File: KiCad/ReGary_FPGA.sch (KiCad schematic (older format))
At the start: 27 parts, among them U1 GW1N-UV1P5LQ100, U2 LM1117-3.3, U9 TPS73643DBV

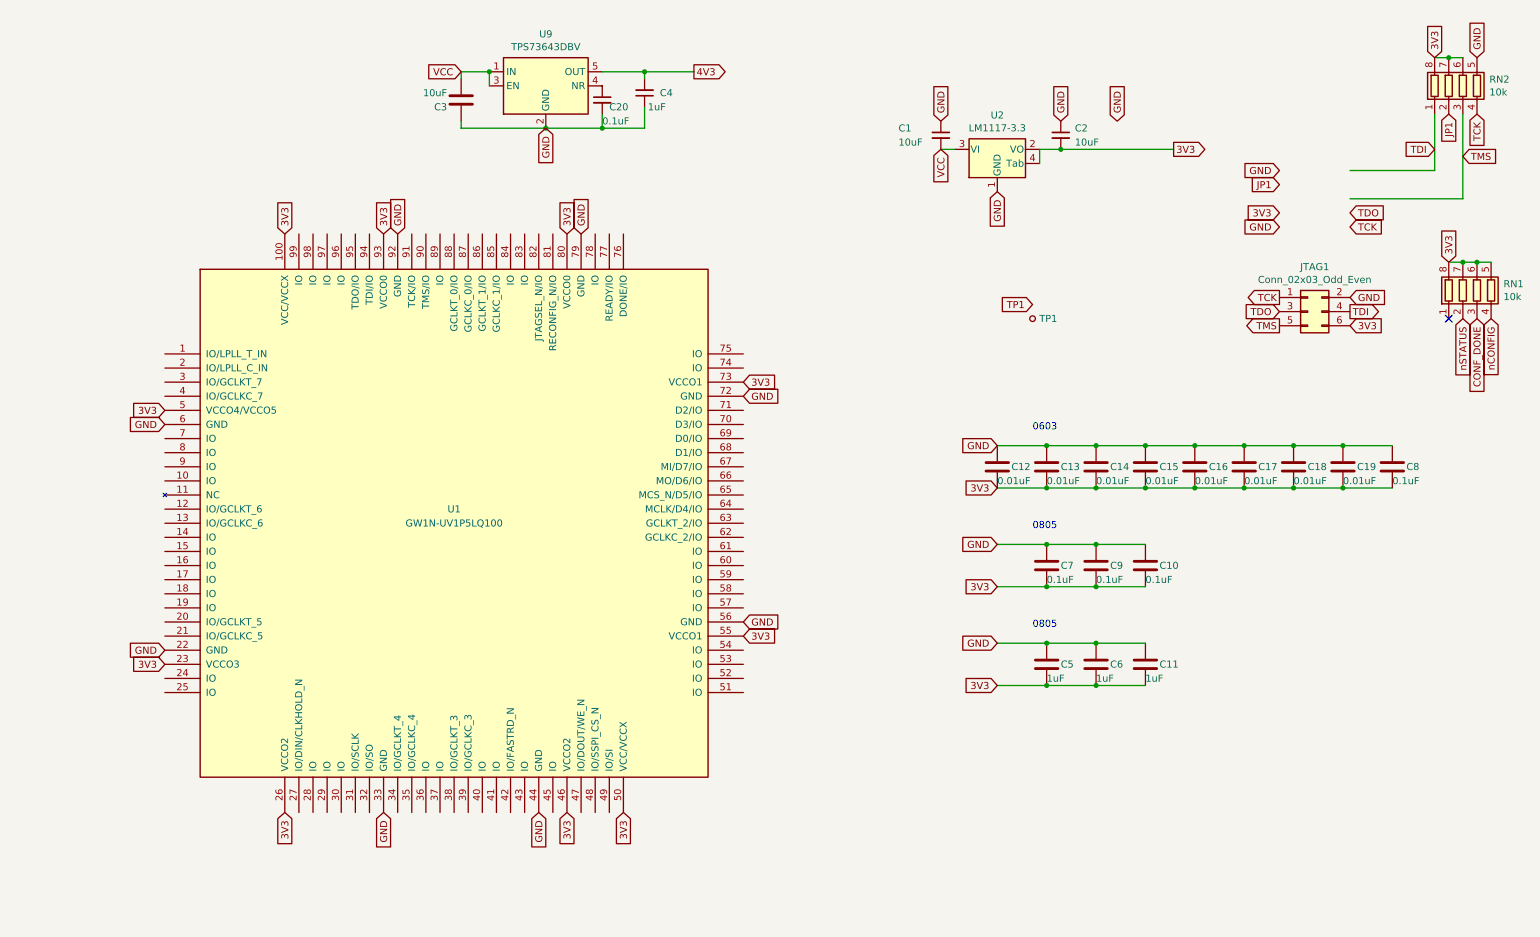
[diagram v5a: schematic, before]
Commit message: fixed placement of capacitors C8 and C9
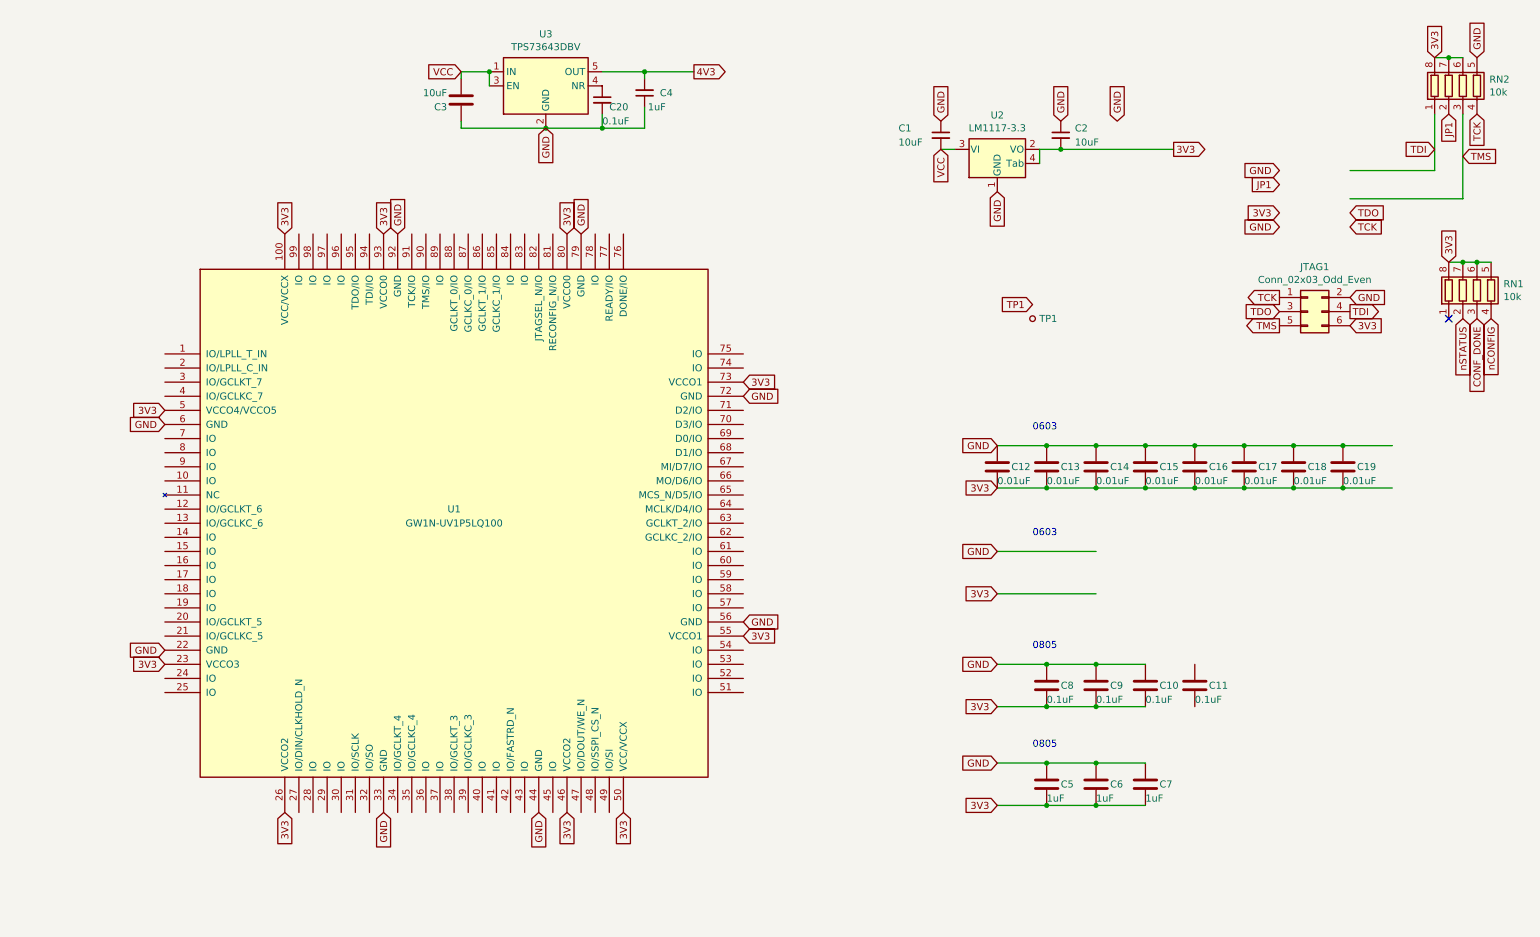
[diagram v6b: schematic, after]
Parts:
- C5, C6, C9: footprint Capacitor_SMD:C_0805_2012Metric_Pad1.15x1.40mm_HandSolder -> Capacitor_SMD:C_0805_2012Metric_Pad1.18x1.45mm_HandSolder
- C7: renamed from C11; footprint Capacitor_SMD:C_0805_2012Metric_Pad1.15x1.40mm_HandSolder -> Capacitor_SMD:C_0805_2012Metric_Pad1.18x1.45mm_HandSolder
- C8: footprint Capacitor_SMD:C_0603_1608Metric_Pad1.05x0.95mm_HandSolder -> Capacitor_SMD:C_0805_2012Metric_Pad1.18x1.45mm_HandSolder
- renumbered C7 to C11, U9 to U3
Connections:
- wire segments 53 -> 55
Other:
- moved on the sheet: C10, C11, C5, C6, C7, C9
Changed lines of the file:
@@
-$Comp
-L Device:C C?
-U 1 1 60CC8EF6
-P 10050 3750
-AR Path="/60CC8EF6" Ref="C?"  Part="1"
-AR Path="/608A10F5/60CC8EF6" Ref="C8"  Part="1"
-F 0 "C8" H 10150 3750 50  0000 L CNN
-F 1 "0.1uF" H 10050 3650 50  0000 L CNN
-F 2 "Capacitor_SMD:C_0603_1608Metric_Pad1.05x0.95mm_HandSolder" H 10088 3600 50  0001 C CNN
-F 3 "~" H 10050 3750 50  0001 C CNN
-	1    10050 3750
-	1    0    0    -1
-$EndComp
 $Comp
 L Device:C C?
@@
 L Device:C C?
 U 1 1 60CC8F0E
-P 8300 4450
+P 8300 5300
 AR Path="/60CC8F0E" Ref="C?"  Part="1"
 AR Path="/608A10F5/60CC8F0E" Ref="C10"  Part="1"
-F 0 "C10" H 8400 4450 50  0000 L CNN
-F 1 "0.1uF" H 8300 4350 50  0000 L CNN
-F 2 "Capacitor_SMD:C_0805_2012Metric_Pad1.15x1.40mm_HandSolder" H 8338 4300 50  0001 C CNN
-F 3 "~" H 8300 4450 50  0001 C CNN
-	1    8300 4450
+F 0 "C10" H 8400 5300 50  0000 L CNN
+F 1 "0.1uF" H 8300 5200 50  0000 L CNN
+F 2 "Capacitor_SMD:C_0805_2012Metric_Pad1.15x1.40mm_HandSolder" H 8338 5150 50  0001 C CNN
+F 3 "~" H 8300 5300 50  0001 C CNN
+	1    8300 5300
 	1    0    0    -1
 $EndComp
@@
 Wire Wire Line
 	7950 3900 8300 3900
-Text GLabel 7250 4600 0    50   Input ~ 0
+Text GLabel 7250 5450 0    50   Input ~ 0
 3V3
 Connection ~ 8300 3600
@@
 L Device:C C?
 U 1 1 607ACE36
-P 7600 4450
+P 8650 5300
 AR Path="/607ACE36" Ref="C?"  Part="1"
-AR Path="/608A10F5/607ACE36" Ref="C7"  Part="1"
-F 0 "C7" H 7700 4450 50  0000 L CNN
-F 1 "0.1uF" H 7600 4350 50  0000 L CNN
-F 2 "Capacitor_SMD:C_0805_2012Metric_Pad1.15x1.40mm_HandSolder" H 7638 4300 50  0001 C CNN
-F 3 "~" H 7600 4450 50  0001 C CNN
-	1    7600 4450
+AR Path="/608A10F5/607ACE36" Ref="C11"  Part="1"
+F 0 "C11" H 8750 5300 50  0000 L CNN
+F 1 "0.1uF" H 8650 5200 50  0000 L CNN
+F 2 "Capacitor_SMD:C_0805_2012Metric_Pad1.15x1.40mm_HandSolder" H 8688 5150 50  0001 C CNN
+F 3 "~" H 8650 5300 50  0001 C CNN
+	1    8650 5300
 	1    0    0    -1
 $EndComp
@@
 Wire Wire Line
 	7250 3600 7600 3600
-Text GLabel 7250 4300 0    50   Input ~ 0
-GND
-Wire Wire Line
-	7250 4300 7600 4300
-Connection ~ 7600 4300
-Wire Wire Line
-	7600 4300 7950 4300
-Wire Wire Line
-	7250 4600 7600 4600
-Connection ~ 7600 4600
-Wire Wire Line
-	7600 4600 7950 4600
+Text GLabel 7250 5150 0    50   Input ~ 0
+GND
 Text GLabel 7250 3900 0    50   Input ~ 0
 3V3
 Text Notes 7500 3500 0    50   ~ 0
 0603
-Text Notes 7500 4200 0    50   ~ 0
+Text Notes 7500 5050 0    50   ~ 0
 0805
 Text GLabel 9250 1750 0    50   Input ~ 0
@@
 L Device:C C?
 U 1 1 608291F3
-P 7950 4450
+P 7950 5300
 AR Path="/608291F3" Ref="C?"  Part="1"
 AR Path="/608A10F5/608291F3" Ref="C9"  Part="1"
-F 0 "C9" H 8050 4450 50  0000 L CNN
-F 1 "0.1uF" H 7950 4350 50  0000 L CNN
-F 2 "Capacitor_SMD:C_0805_2012Metric_Pad1.15x1.40mm_HandSolder" H 7988 4300 50  0001 C CNN
-F 3 "~" H 7950 4450 50  0001 C CNN
-	1    7950 4450
-	1    0    0    -1
-$EndComp
-Wire Wire Line
-	7950 4300 8300 4300
-Connection ~ 7950 4300
-Wire Wire Line
-	7950 4600 8300 4600
-Connection ~ 7950 4600
+F 0 "C9" H 8050 5300 50  0000 L CNN
+F 1 "0.1uF" H 7950 5200 50  0000 L CNN
+F 2 "Capacitor_SMD:C_0805_2012Metric_Pad1.18x1.45mm_HandSolder" H 7988 5150 50  0001 C CNN
+F 3 "~" H 7950 5300 50  0001 C CNN
+	1    7950 5300
+	1    0    0    -1
+$EndComp
+Wire Wire Line
+	7950 5150 8300 5150
+Connection ~ 7950 5150
+Wire Wire Line
+	7950 5450 8300 5450
+Connection ~ 7950 5450
 $Comp
 L Device:C C?
@@
 L Device:C C?
 U 1 1 608425C5
-P 7600 5150
+P 7600 6000
 AR Path="/608425C5" Ref="C?"  Part="1"
 AR Path="/608A10F5/608425C5" Ref="C5"  Part="1"
-F 0 "C5" H 7700 5150 50  0000 L CNN
-F 1 "1uF" H 7600 5050 50  0000 L CNN
-F 2 "Capacitor_SMD:C_0805_2012Metric_Pad1.15x1.40mm_HandSolder" H 7638 5000 50  0001 C CNN
-F 3 "~" H 7600 5150 50  0001 C CNN
-	1    7600 5150
+F 0 "C5" H 7700 6000 50  0000 L CNN
+F 1 "1uF" H 7600 5900 50  0000 L CNN
+F 2 "Capacitor_SMD:C_0805_2012Metric_Pad1.18x1.45mm_HandSolder" H 7638 5850 50  0001 C CNN
+F 3 "~" H 7600 6000 50  0001 C CNN
+	1    7600 6000
 	1    0    0    -1
 $EndComp
@@
 L Device:C C?
 U 1 1 6084338C
-P 7950 5150
+P 7950 6000
 AR Path="/6084338C" Ref="C?"  Part="1"
 AR Path="/608A10F5/6084338C" Ref="C6"  Part="1"
-F 0 "C6" H 8050 5150 50  0000 L CNN
-F 1 "1uF" H 7950 5050 50  0000 L CNN
-F 2 "Capacitor_SMD:C_0805_2012Metric_Pad1.15x1.40mm_HandSolder" H 7988 5000 50  0001 C CNN
-F 3 "~" H 7950 5150 50  0001 C CNN
-	1    7950 5150
+F 0 "C6" H 8050 6000 50  0000 L CNN
+F 1 "1uF" H 7950 5900 50  0000 L CNN
+F 2 "Capacitor_SMD:C_0805_2012Metric_Pad1.18x1.45mm_HandSolder" H 7988 5850 50  0001 C CNN
+F 3 "~" H 7950 6000 50  0001 C CNN
+	1    7950 6000
 	1    0    0    -1
 $EndComp
@@
 L Device:C C?
 U 1 1 6084459F
-P 8300 5150
+P 8300 6000
 AR Path="/6084459F" Ref="C?"  Part="1"
-AR Path="/608A10F5/6084459F" Ref="C11"  Part="1"
-F 0 "C11" H 8400 5150 50  0000 L CNN
-F 1 "1uF" H 8300 5050 50  0000 L CNN
-F 2 "Capacitor_SMD:C_0805_2012Metric_Pad1.15x1.40mm_HandSolder" H 8338 5000 50  0001 C CNN
-F 3 "~" H 8300 5150 50  0001 C CNN
-	1    8300 5150
+AR Path="/608A10F5/6084459F" Ref="C7"  Part="1"
+F 0 "C7" H 8400 6000 50  0000 L CNN
+F 1 "1uF" H 8300 5900 50  0000 L CNN
+F 2 "Capacitor_SMD:C_0805_2012Metric_Pad1.18x1.45mm_HandSolder" H 8338 5850 50  0001 C CNN
+F 3 "~" H 8300 6000 50  0001 C CNN
+	1    8300 6000
 	1    0    0    -1
 $EndComp
@@
 	1    0    0    -1
 $EndComp
-Text GLabel 7250 5300 0    50   Input ~ 0
-3V3
-Text GLabel 7250 5000 0    50   Input ~ 0
-GND
-Wire Wire Line
-	7250 5000 7600 5000
-Wire Wire Line
-	7250 5300 7600 5300
-Text Notes 7500 4900 0    50   ~ 0
+Text GLabel 7250 6150 0    50   Input ~ 0
+3V3
+Text GLabel 7250 5850 0    50   Input ~ 0
+GND
+Wire Wire Line
+	7250 5850 7600 5850
+Wire Wire Line
+	7250 6150 7600 6150
+Text Notes 7500 5750 0    50   ~ 0
 0805
 Wire Wire Line
-	7600 5000 7950 5000
-Connection ~ 7600 5000
-Wire Wire Line
-	7950 5000 8300 5000
-Connection ~ 7950 5000
-Wire Wire Line
-	7600 5300 7950 5300
-Connection ~ 7600 5300
-Connection ~ 7950 5300
-Wire Wire Line
-	7950 5300 8300 5300
+	7600 5850 7950 5850
+Connection ~ 7600 5850
+Wire Wire Line
+	7950 5850 8300 5850
+Connection ~ 7950 5850
+Wire Wire Line
+	7600 6150 7950 6150
+Connection ~ 7600 6150
+Connection ~ 7950 6150
+Wire Wire Line
+	7950 6150 8300 6150
 $Comp
 L ReGary:GW1N-UV1P5LQ100 U1
@@
 3V3
 $Comp
-L Regulator_Linear:TPS73643DBV U9
+L Regulator_Linear:TPS73643DBV U3
 U 1 1 67D103CA
 P 4050 1050
-F 0 "U9" H 4050 1417 50  0000 C CNN
+F 0 "U3" H 4050 1417 50  0000 C CNN
 F 1 "TPS73643DBV" H 4050 1326 50  0000 C CNN
 F 2 "Package_TO_SOT_SMD:SOT-23-5" H 4050 1375 50  0001 C CIN
@@
 Wire Wire Line
 	4450 1350 4750 1350
+Text GLabel 7250 4650 0    50   Input ~ 0
+3V3
+Text GLabel 7250 4350 0    50   Input ~ 0
+GND
+Text Notes 7500 4250 0    50   ~ 0
+0603
+Wire Wire Line
+	7250 4350 7950 4350
+Wire Wire Line
+	7250 4650 7950 4650
+$Comp
+L Device:C C?
+U 1 1 67F0E861
+P 7600 5300
+AR Path="/67F0E861" Ref="C?"  Part="1"
+AR Path="/608A10F5/67F0E861" Ref="C8"  Part="1"
+F 0 "C8" H 7700 5300 50  0000 L CNN
+F 1 "0.1uF" H 7600 5200 50  0000 L CNN
+F 2 "Capacitor_SMD:C_0805_2012Metric_Pad1.18x1.45mm_HandSolder" H 7638 5150 50  0001 C CNN
+F 3 "~" H 7600 5300 50  0001 C CNN
+	1    7600 5300
+	1    0    0    -1
+$EndComp
+Wire Wire Line
+	7250 5150 7600 5150
+Wire Wire Line
+	7250 5450 7600 5450
+Connection ~ 7600 5150
+Wire Wire Line
+	7600 5150 7950 5150
+Connection ~ 7600 5450
+Wire Wire Line
+	7600 5450 7950 5450
 $EndSCHEMATC

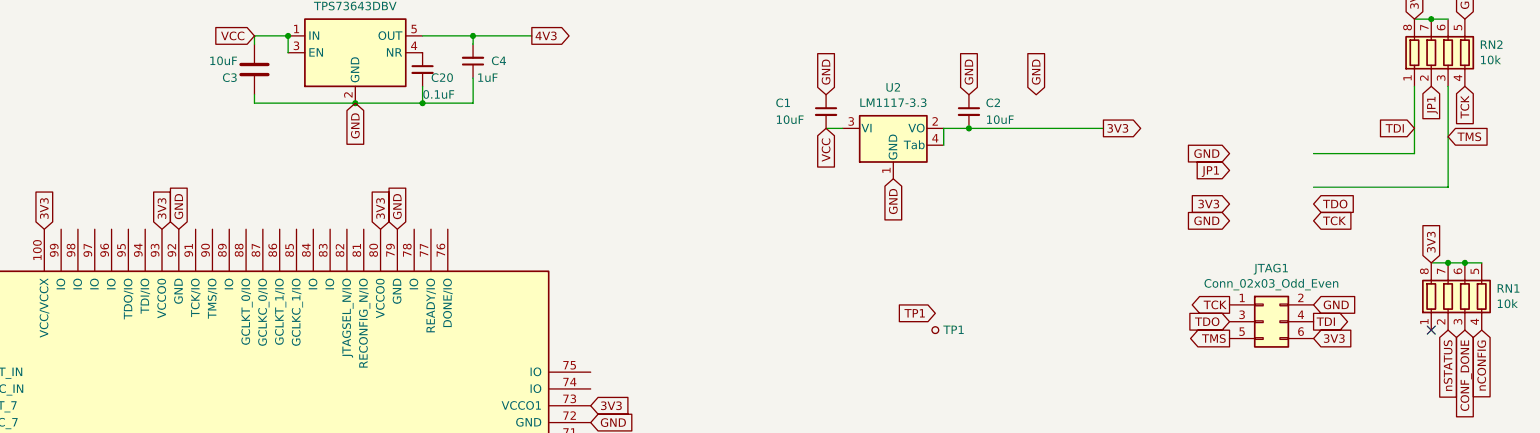
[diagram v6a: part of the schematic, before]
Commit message: Add JTAG routing and 4.7k pull-down resistor on TCK-line
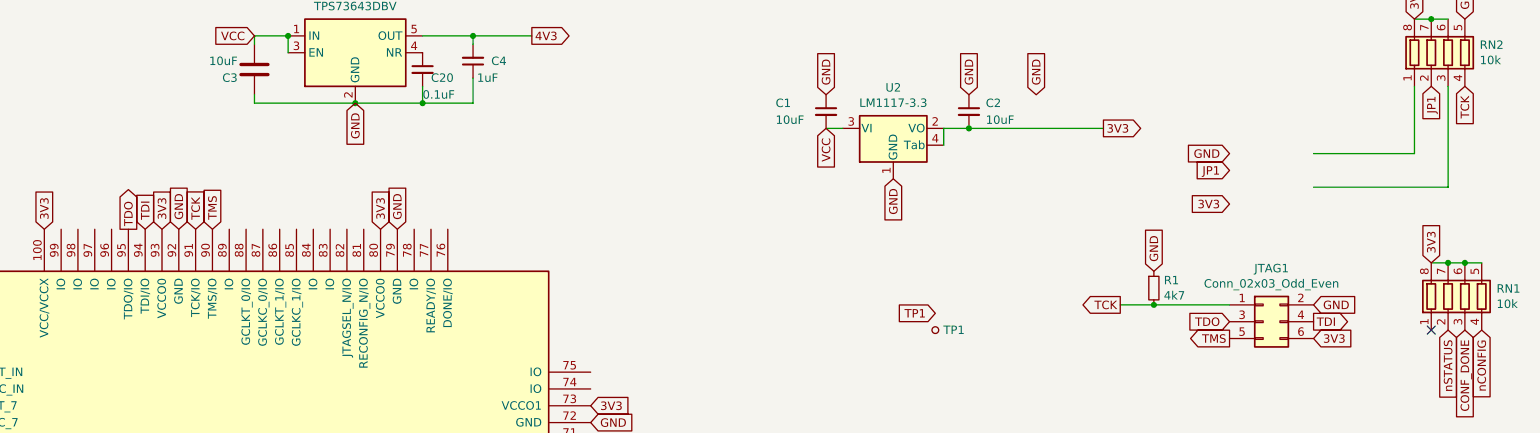
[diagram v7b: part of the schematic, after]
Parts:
- added R1: 4k7, Resistor_SMD:R_0603_1608Metric_Pad0.98x0.95mm_HandSolder, symbol Device:R_Small
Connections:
- wire segments 55 -> 57
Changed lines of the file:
@@
 Text GLabel 9250 1950 0    50   Input ~ 0
 3V3
-Text GLabel 9250 2050 0    50   Input ~ 0
-GND
-Text GLabel 10350 1500 0    50   Input ~ 0
+Text GLabel 8800 2350 1    50   Input ~ 0
+GND
+Text GLabel 2800 2100 1    50   Input ~ 0
 TDI
-Text GLabel 10550 1550 2    50   Input ~ 0
+Text GLabel 3200 2100 1    50   Input ~ 0
 TMS
-Text GLabel 9750 1950 2    50   Input ~ 0
+Text GLabel 2700 2100 1    50   Output ~ 0
 TDO
 Text GLabel 10350 850  1    50   Input ~ 0
@@
 Text GLabel 10650 1250 3    50   Input ~ 0
 TCK
-Text GLabel 9750 2050 2    50   Input ~ 0
+Text GLabel 3100 2100 1    50   Input ~ 0
 TCK
 $Comp
@@
 	1    0    0    -1
 $EndComp
-Text GLabel 9250 2550 0    50   Output ~ 0
+Text GLabel 8600 2550 0    50   Output ~ 0
 TCK
 Text GLabel 9250 2650 0    50   Input ~ 0
@@
 Wire Wire Line
 	7600 5450 7950 5450
+$Comp
+L Device:R_Small R1
+U 1 1 67F65041
+P 8800 2450
+F 0 "R1" H 8859 2496 50  0000 L CNN
+F 1 "4k7" H 8859 2405 50  0000 L CNN
+F 2 "Resistor_SMD:R_0603_1608Metric_Pad0.98x0.95mm_HandSolder" H 8800 2450 50  0001 C CNN
+F 3 "~" H 8800 2450 50  0001 C CNN
+	1    8800 2450
+	1    0    0    -1
+$EndComp
+Wire Wire Line
+	9250 2550 8800 2550
+Connection ~ 8800 2550
+Wire Wire Line
+	8800 2550 8600 2550
 $EndSCHEMATC
